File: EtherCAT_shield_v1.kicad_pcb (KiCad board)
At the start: 2 copper layers, 73.7 x 81.3 mm, 69 parts, among them J1 RJ45-PULSETRANS, J2 RJ45-PULSETRANS, P1 CONN_02X10, P2 CONN_02X19, P3 CONN_02X19, U1 LAN9252, U2 24LC00, Y1 Crystal_GND24

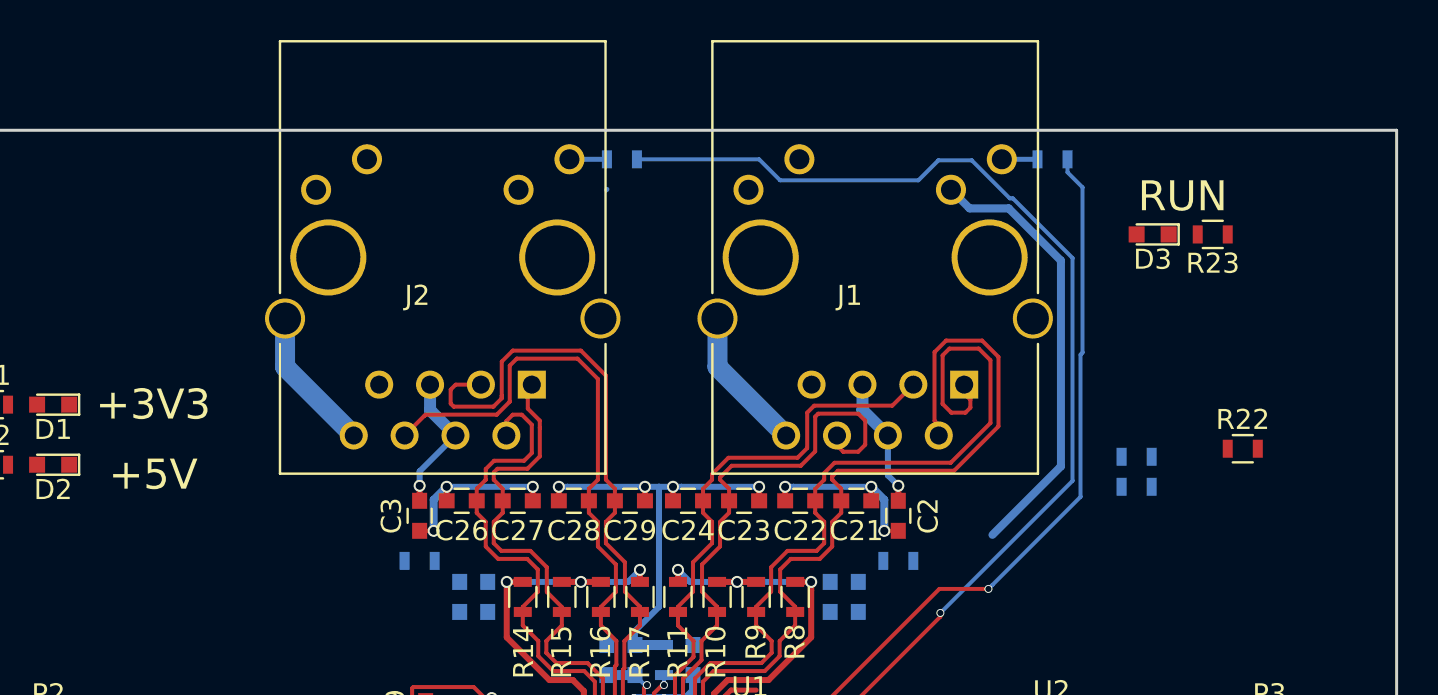
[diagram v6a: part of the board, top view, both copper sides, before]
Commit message: LINK方向の矢印追加
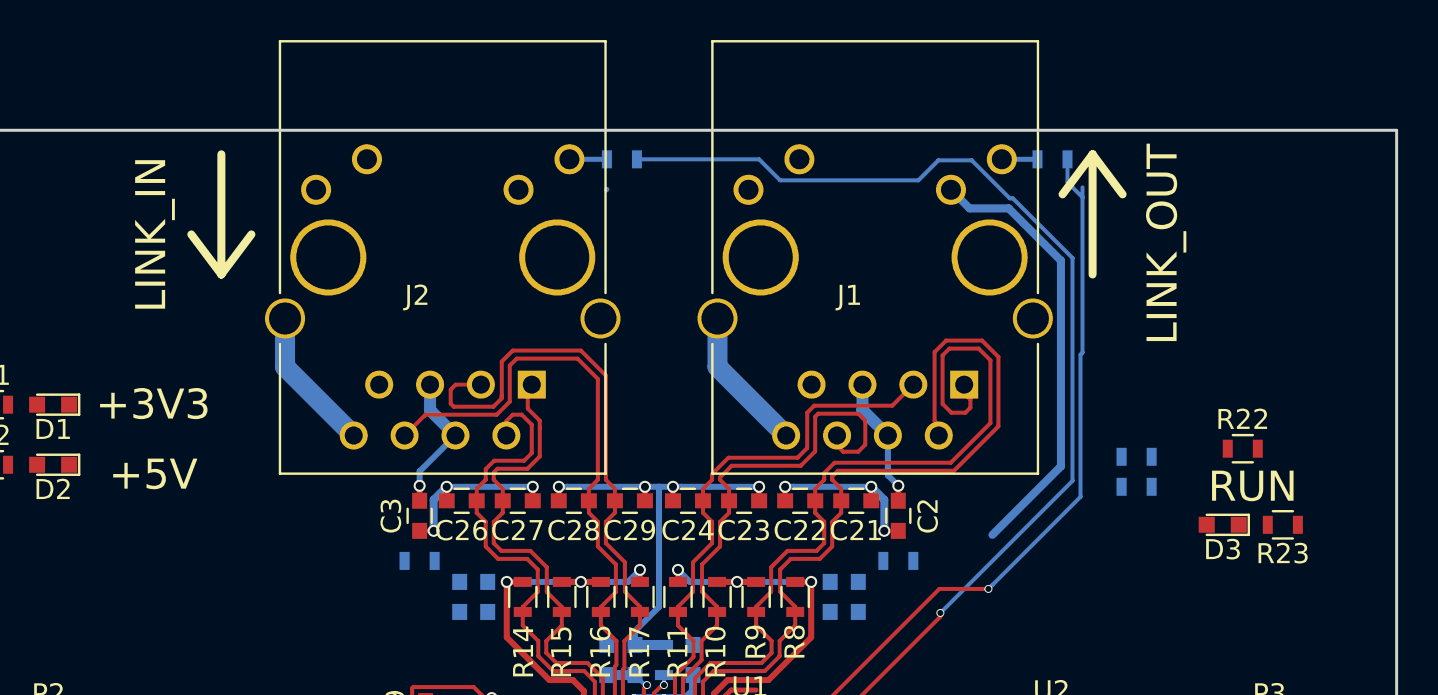
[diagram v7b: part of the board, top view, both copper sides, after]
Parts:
- moved D3 14.9 mm to (161.5, 70.5)
- moved R23 14.9 mm to (164.5, 70.5)
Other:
- board text added: "LINK_IN"
- board text added: "LINK_OUT"
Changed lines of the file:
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@@
   (general
     (links 207)
-    (no_connects 146)
+    (no_connects 141)
     (area 96.444999 50.724999 170.255001 132.155001)
     (thickness 1.6)
-    (drawings 10)
+    (drawings 18)
     (tracks 437)
     (zones 0)
@@
   )
   (setup
-    (last_trace_width 0.4)
+    (last_trace_width 1)
     (user_trace_width 0.2)
     (user_trace_width 0.3)
@@
   )
   (module LEDs:LED_0603 (layer F.Cu)
-    (at 158 56 180)
+    (at 161.5 70.5 180)
     (descr "LED 0603 smd package")
     (tags "LED led 0603 SMD smd SMT smt smdled SMDLED smtled SMTLED")
@@
   )
   (module Resistors_SMD:R_0603 (layer F.Cu)
-    (at 161 56 180)
+    (at 164.5 70.5 180)
     (descr "Resistor SMD 0603, reflow soldering, Vishay (see dcrcw.pdf)")
     (tags "resistor 0603")
@@
       (net 2 GND))
   )
-  (gr_text RUN (at 159.5 54.1) (layer F.SilkS)
+  (gr_line (start 111.5 58) (end 111.5 52) (layer F.SilkS) (width 0.4))
+  (gr_line (start 113 56) (end 111.5 58) (layer F.SilkS) (width 0.4))
+  (gr_line (start 111.5 58) (end 110 56) (layer F.SilkS) (width 0.4))
+  (gr_line (start 155 52) (end 156.5 54) (layer F.SilkS) (width 0.4))
+  (gr_line (start 153.5 54) (end 155 52) (layer F.SilkS) (width 0.4))
+  (gr_line (start 155 52) (end 155 58) (layer F.SilkS) (width 0.4))
+  (gr_text LINK_OUT (at 158.5 56.5 90) (layer F.SilkS)
+    (effects (font (size 1.5 1.5) (thickness 0.3)))
+  )
+  (gr_text LINK_IN (at 108 56 90) (layer F.SilkS)
+    (effects (font (size 1.5 1.5) (thickness 0.3)))
+  )
+  (gr_text RUN (at 163 68.6) (layer F.SilkS)
     (effects (font (size 1.5 1.5) (thickness 0.3)))
   )
@@
   (segment (start 147.35 73.7) (end 149.8 73.7) (width 0.2) (layer F.Cu) (net 36))
   (via (at 149.8 73.7) (size 0.4) (drill 0.3) (layers F.Cu B.Cu) (net 36))
-  (segment (start 153.75 52.25) (end 153.75 52.9) (width 0.2) (layer B.Cu) (net 36))
-  (segment (start 153.75 52.9) (end 154.5 53.65) (width 0.2) (layer B.Cu) (net 36))
+  (segment (start 153.75 52.75) (end 153.75 53.4) (width 0.2) (layer B.Cu) (net 36))
+  (segment (start 153.75 53.4) (end 154.5 54.15) (width 0.2) (layer B.Cu) (net 36))
   (segment (start 139 82.05) (end 147.35 73.7) (width 0.2) (layer F.Cu) (net 36))
   (segment (start 138.525 80.6) (end 139 80.6) (width 0.2) (layer F.Cu) (net 36))

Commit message: 画像はりたい
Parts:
- moved C5 41.6 mm to (139.9, 80.2), turned to 90 degrees
- moved C19 3.35 mm to (121.1, 76.8)
- moved C20 3.35 mm to (121.1, 79.8)
- moved Y1 3.35 mm to (123.6, 78.2)
- moved R18 1.80 mm to (125.1, 84.2)
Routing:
- net GND: track 102.6 -> 139.6 mm
- net (no net): track 0.03 -> 26.2 mm, vias 0 -> 1
- net /LAN9252/LINKACTLED0: track 39.2 -> 17.3 mm, vias 1 -> 0
- net Net-(C19-Pad1): track 8.62 -> 10.0 mm
- net +3V3: track 1.15 -> 0.00 mm, vias 1 -> 0
- net /LAN9252/LINKACTLED1: track 58.3 -> 57.5 mm
- net Net-(P3-Pad17): track 2.64 -> 3.35 mm, vias 0 -> 1
- net Net-(P1-Pad9): track 1.78 -> 2.25 mm, vias 0 -> 1
